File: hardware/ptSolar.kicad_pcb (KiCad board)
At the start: 4 copper layers, 38 x 73.5 mm, 52 parts, among them J3 Conn_01x03, J4 ICSP, J5 Qwiic, U2 SA818S-V, U3 TXB0104D, U4 BME280, U5 LP3985IM5-3.3/NOPB, U7 MEGA8-AI, Y2 8MHz

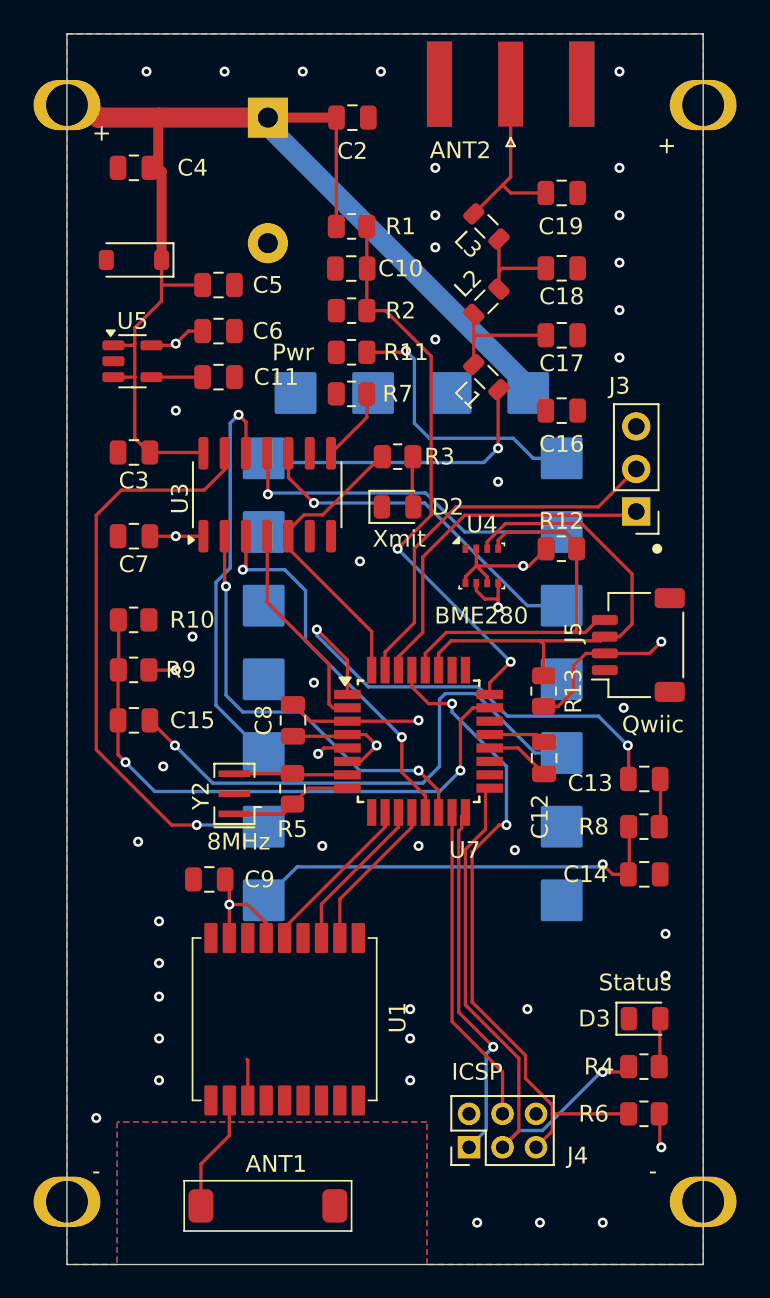
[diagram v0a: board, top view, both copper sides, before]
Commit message: Updated to PCB 1.1.0. Firmware mostly validated. Switched to FET-based level translators.
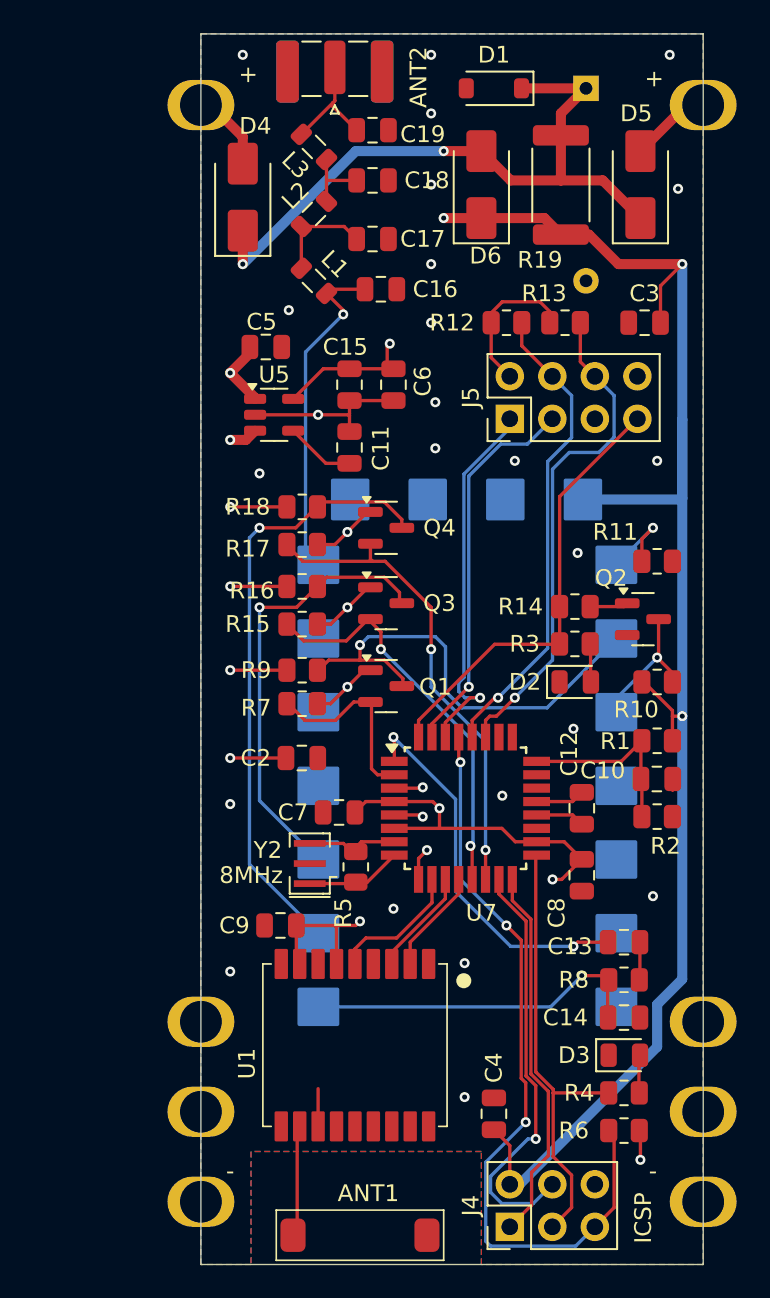
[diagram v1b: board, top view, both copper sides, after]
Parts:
- removed J3: Conn_01x03, Connector_PinHeader_2.54mm:PinHeader_1x03_P2.54mm_Vertical
- removed U3: TXB0104D, Package_SO:SOIC-14_3.9x8.7mm_P1.27mm
- removed U4: BME280, Package_LGA:Bosch_LGA-8_2.5x2.5mm_P0.65mm_ClockwisePinNumbering
- added D4: D_Schottky, Diode_SMD:D_SMA, F.Cu at (139.8, 77.5)
- added D5: D_Schottky, Diode_SMD:D_SMA, F.Cu at (163.5, 76.8)
- added D6: D_Schottky, Diode_SMD:D_SMA, F.Cu at (154.0, 76.8)
- added Q1: BSS138, Package_TO_SOT_SMD:SOT-23, F.Cu at (148.3, 106.7)
- added Q2: MMBT3904, Package_TO_SOT_SMD:SOT-23, F.Cu at (163.7, 102.7)
- added Q3: BSS138, Package_TO_SOT_SMD:SOT-23, F.Cu at (148.3, 101.8)
- added Q4: BSS138, Package_TO_SOT_SMD:SOT-23, F.Cu at (148.3, 97.2)
- added R14: 1k, Resistor_SMD:R_0805_2012Metric, F.Cu at (159.6, 102.0)
- added R15: 10k, Resistor_SMD:R_0805_2012Metric, F.Cu at (143.3, 103.0)
- added R16: 10k, Resistor_SMD:R_0805_2012Metric, F.Cu at (143.3, 100.8)
- added R17: 10k, Resistor_SMD:R_0805_2012Metric, F.Cu at (143.3, 98.2)
- added R18: 10k, Resistor_SMD:R_0805_2012Metric, F.Cu at (143.3, 96.0)
- added R19: 47, Resistor_SMD:R_2512_6332Metric, F.Cu at (158.8, 76.8)
- ANT2: value Conn_Coaxial_Power -> SMA Edge Mount (Optional); footprint Connector_Coaxial:SMA_Amphenol_132289_EdgeMount -> Connector_Coaxial:SMA_Samtec_SMA-J-P-H-ST-EM1_EdgeMount
- C1: value 6V 2.5F -> 6V 1F; footprint Capacitor_THT:CP_Radial_D16.0mm_P7.50mm -> Custom DS:CDS CSP Super Cap 8mm dia
- C13: value 10nF -> .1uF
- C15: value 10nF -> 2.2uF
- J4: value ICSP -> 6 Pin Male Header; footprint Connector_PinHeader_2.00mm:PinHeader_2x03_P2.00mm_Vertical -> Connector_PinHeader_2.54mm:PinHeader_2x03_P2.54mm_Vertical
- J5: value Qwiic -> Conn_02x04_Odd_Even; footprint Connector_JST:JST_SH_SM04B-SRSS-TB_1x04-1MP_P1.00mm_Horizontal -> Connector_PinHeader_2.54mm:PinHeader_2x04_P2.54mm_Vertical
- R11: value 1M -> 10k
- R8: value 1M -> 4.7k
- U1: value ~ -> ATGM336H-5N31
- moved C4 60.5 mm to (154.8, 132.2), turned to 90 degrees
- moved C2 38.4 mm to (143.3, 111.0)
- moved R1 35.7 mm to (164.5, 110.0), turned to 0 degrees
- moved C10 35.5 mm to (164.5, 112.2), turned to 0 degrees
- moved R2 35.3 mm to (164.5, 114.5), turned to 180 degrees
- moved R10 31.5 mm to (164.5, 106.5), turned to 180 degrees
- moved C3 31.5 mm to (163.8, 85.0)
- moved C15 23.8 mm to (146.1, 88.7), turned to -90 degrees
- moved D1 23.8 mm to (154.8, 71.0)
- moved R11 22.1 mm to (164.5, 99.2), turned to 180 degrees
- moved R13 22.0 mm to (159.0, 85.0), turned to 0 degrees
- moved C7 20.6 mm to (145.5, 114.2)
- moved C8 19.6 mm to (160.0, 118.0), turned to -90 degrees
- moved C1 19.4 mm to (160.2, 76.8), turned to 180 degrees
- moved R7 18.7 mm to (143.3, 107.8)
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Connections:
- C1 pad 1: +BATT -> Net-(D1-K)
- C15 pad 1: Net-(U7-PC0) -> +3.3V
- C15 pad 2: Net-(U2-AF-OUT) -> GND
- D1 pad 1: +BATT -> Net-(D1-K)
- J1 pad 1: +BATT -> Net-(D4-A)
- J2 pad 1: +BATT -> Net-(D5-A)
- J5 pad 1: GND -> Net-(J5-Pin_1)
- J5 pad 3: /SDA -> Net-(J5-Pin_3)
- R10 pad 1: Net-(U7-PC0) -> Net-(Q2-C)
- R10 pad 2: GND -> +BATT
- R7 pad 1: GND -> Net-(Q1-S)
- R7 pad 2: Net-(U3-OE) -> +3.3V
- R9 pad 1: +3.3V -> Net-(Q1-D)
- R9 pad 2: Net-(U7-PC0) -> +BATT
- U2 pad 3: Net-(U2-AF-OUT) -> unconnected-(U2-AF-OUT-Pad3)
- U2 pad 5: Net-(U2-PTT) -> Net-(Q2-C)
- U2 pad 6: Net-(U2-POWER_SAVE) -> Net-(Q1-D)
- U7 pad 18: unconnected-(U7-AVCC-Pad18) -> +3.3V
- U7 pad 2: Net-(U3-A3) -> Net-(Q1-S)
- U7 pad 23: Net-(U7-PC0) -> unconnected-(U7-PC0-Pad23)
- U7 pad 30: Net-(J3-Pin_1) -> Net-(J5-Pin_1)
- U7 pad 31: Net-(J3-Pin_2) -> Net-(J5-Pin_3)
- U7 pad 9: unconnected-(U7-PD5-Pad9) -> Net-(J5-Pin_8)
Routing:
- net Net-(D1-K): track 0.00 -> 40.2 mm, vias 0 -> 2
- net Net-(J5-Pin_8): track 0.00 -> 37.5 mm, vias 0 -> 1
- net Net-(U7-PC0): track 35.7 -> 0.00 mm, vias 2 -> 0
- net Net-(U2-AF-OUT): track 33.4 -> 0.00 mm, vias 1 -> 0
- net Net-(Q1-D): track 0.00 -> 27.6 mm, vias 0 -> 1
- net Net-(J3-Pin_2): track 23.2 -> 0.00 mm
- net /BATT-SENSE: track 34.4 -> 11.4 mm, vias 2 -> 0
- net Net-(J5-Pin_3): track 0.00 -> 22.9 mm, vias 0 -> 1
- net +BATT: track 182.3 -> 159.6 mm, vias 0 -> 9
- net Net-(J5-Pin_1): track 0.00 -> 22.5 mm, vias 0 -> 1
- net Net-(J3-Pin_1): track 21.2 -> 0.00 mm
- net Net-(U2-POWER_SAVE): track 21.0 -> 0.00 mm, vias 1 -> 0
- net Net-(U2-PTT): track 20.9 -> 0.00 mm, vias 1 -> 0
- net +3.3V: track 43.0 -> 60.9 mm
- net Net-(U3-A3): track 12.7 -> 0.00 mm
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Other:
- board size 38 x 73.5 mm -> 30 x 73.5 mm
- board text added: "ICSP"
- board text added: "ptSolar Tracker v1.1.0 Custom Digital Services, LLC www.custom-ds.com"
- board text removed: "Pwr"
- board text removed: "Status"
- board text removed: "Xmit"
- board text removed: "ptSolar Tracker v1.0.0 Custom Digital Services, LLC www.custom-ds.com"
